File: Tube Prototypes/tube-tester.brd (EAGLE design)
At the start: 100 x 75 mm, 37 parts, among them IC1 NE555D, IC2 74141N, IC3 7805, Q1 IRF740S, Q2 BC546

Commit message: new tester board
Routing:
- net N$29: track 157.8 -> 97.4 mm, vias 2 -> 1
- net GND: track 275.8 -> 229.1 mm, vias 4 -> 1
- net N$23: track 52.3 -> 89.7 mm, vias 1 -> 2
- net N$10: track 21.9 -> 41.8 mm
- net N$7: track 120.3 -> 100.4 mm, vias 0 -> 1
- net N$1: track 34.4 -> 15.2 mm
- net N$20: track 55.2 -> 40.8 mm, vias 0 -> 1
- net N$6: track 85.6 -> 71.4 mm, vias 0 -> 1
- net N$30: track 48.8 -> 35.6 mm, vias 0 -> 1
- net N$13: track 16.4 -> 28.5 mm, vias 0 -> 1
- net N$11: track 21.5 -> 33.2 mm, vias 0 -> 1
- net N$24: track 43.9 -> 55.1 mm, vias 1 -> 2
- net N$22: track 84.9 -> 75.4 mm, vias 1 -> 2
- net N$25: track 43.0 -> 33.9 mm
- net N$14: track 23.9 -> 32.9 mm
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
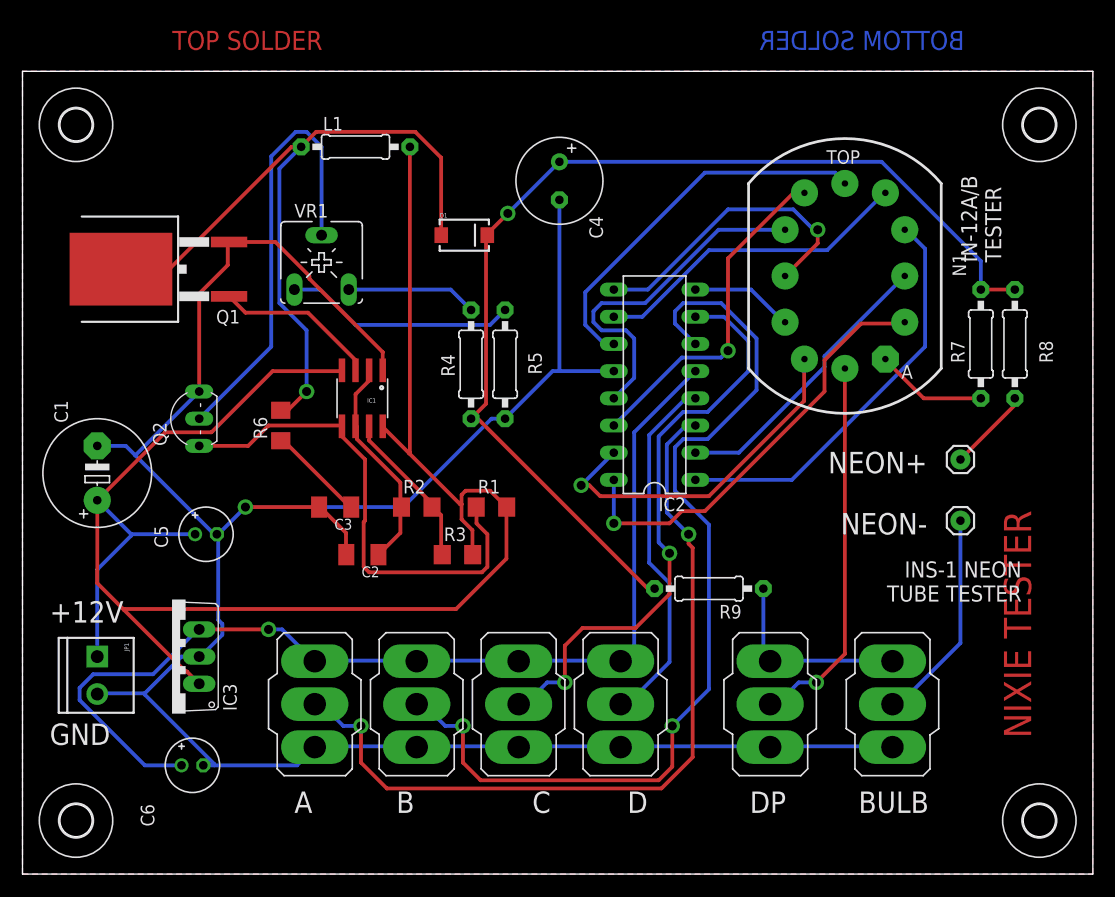
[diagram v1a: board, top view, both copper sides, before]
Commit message: new 180V and tube tester
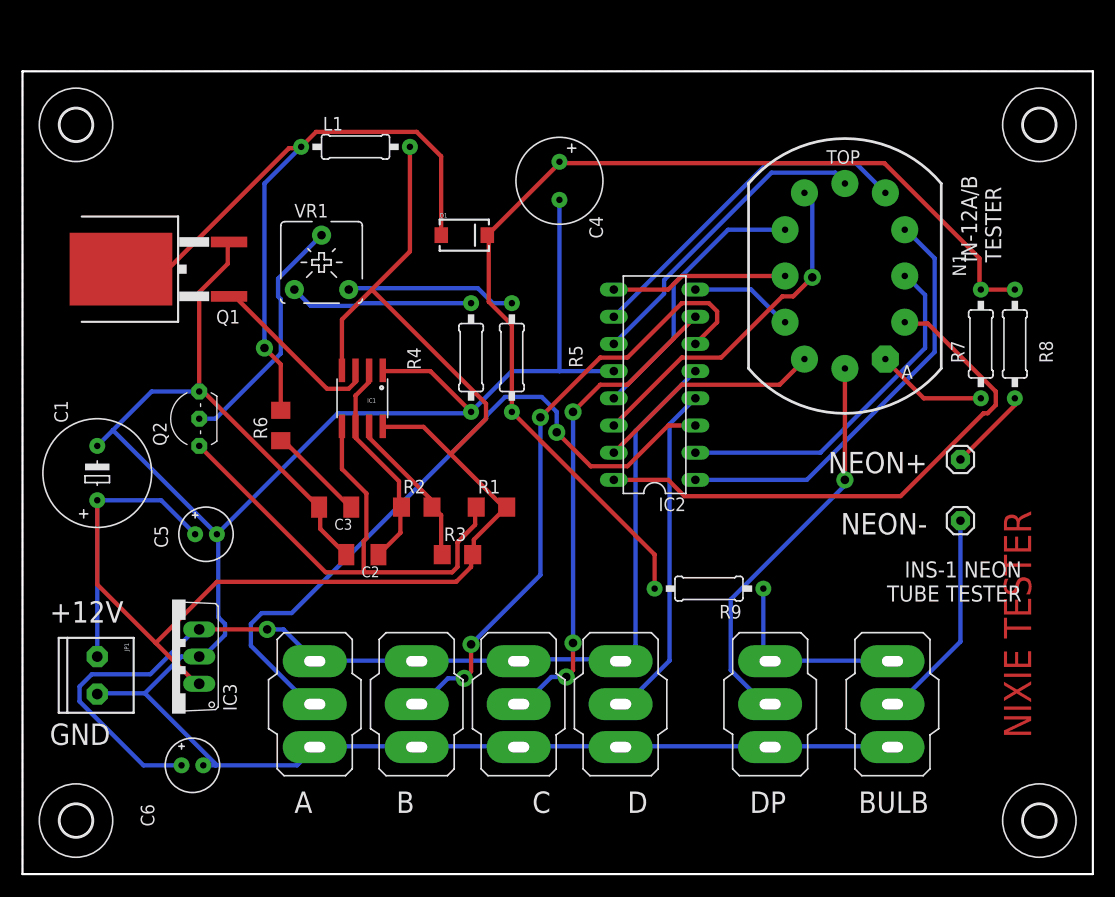
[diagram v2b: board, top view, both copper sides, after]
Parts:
- N1: value IN-12BIN-12 -> IN-12B
- Q2: device iStivi - Transistor-FET:TO92-EBC -> iStivi - Transistor-FET-reg:TO92-EBC
- moved R5 3.86 mm to (45.7, 48.3)
- moved R4 3.24 mm to (41.9, 48.3)
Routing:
- net N$23: track 89.7 -> 57.9 mm, vias 2 -> 3
- net N$26: track 165.0 -> 145.2 mm
- net N$10: track 41.8 -> 23.0 mm
- net N$13: track 28.5 -> 16.5 mm, vias 1 -> 0
- net N$11: track 33.2 -> 21.5 mm, vias 1 -> 0
- net N$20: track 40.8 -> 52.3 mm, vias 1 -> 0
- net N$24: track 55.1 -> 45.6 mm, vias 2 -> 3
- net N$22: track 75.4 -> 66.1 mm, vias 2 -> 1
- net N$14: track 32.9 -> 25.5 mm
- net N$16: track 35.8 -> 29.5 mm
- net N$19: track 27.0 -> 33.1 mm
- net N$9: track 21.6 -> 17.2 mm
- net N$3: track 46.2 -> 50.3 mm
- net N$8: track 12.2 -> 15.9 mm
- net N$17: track 30.2 -> 32.5 mm
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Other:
- board text removed: "A"
- board text removed: "BOTTOM MASK"
- board text removed: "BOTTOM SOLDER"
- board text removed: "TOP"
- board text removed: "TOP MASK"
- board text removed: "TOP SOLDER"
